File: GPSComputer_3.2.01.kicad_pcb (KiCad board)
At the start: 4 copper layers, 96 x 96 mm, 80 parts, among them J1 GPS_ANT_0, J2 GPS_ANT_0, J3 GPS_ANT_0, J4 2125281600, J5 Conn_02x08_Odd_Even, J6 Conn_02x08_Odd_Even, J7 GPS_ANT_0, U1 MAX-M10S-00B, U2 MAX-M10S-00B, U3 MAX-M10S-00B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

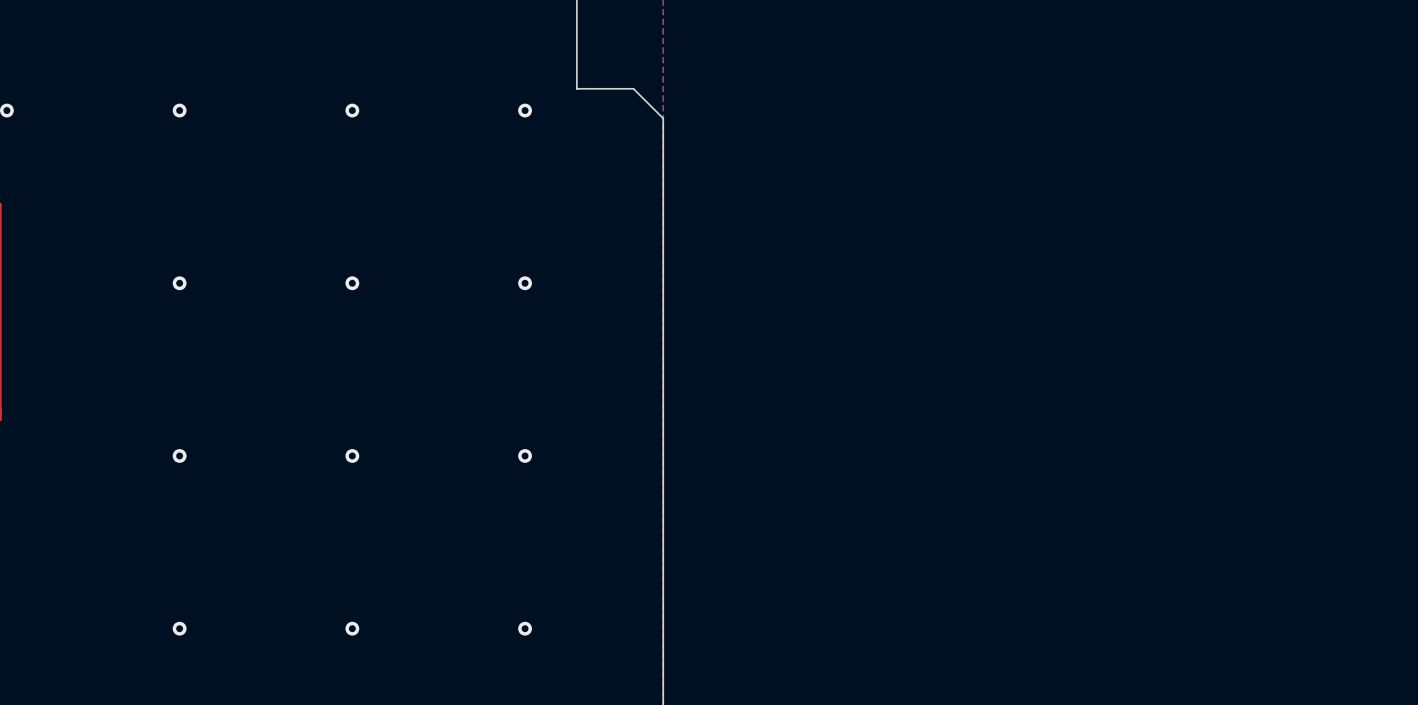
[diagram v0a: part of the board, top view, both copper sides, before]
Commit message: Adding RF
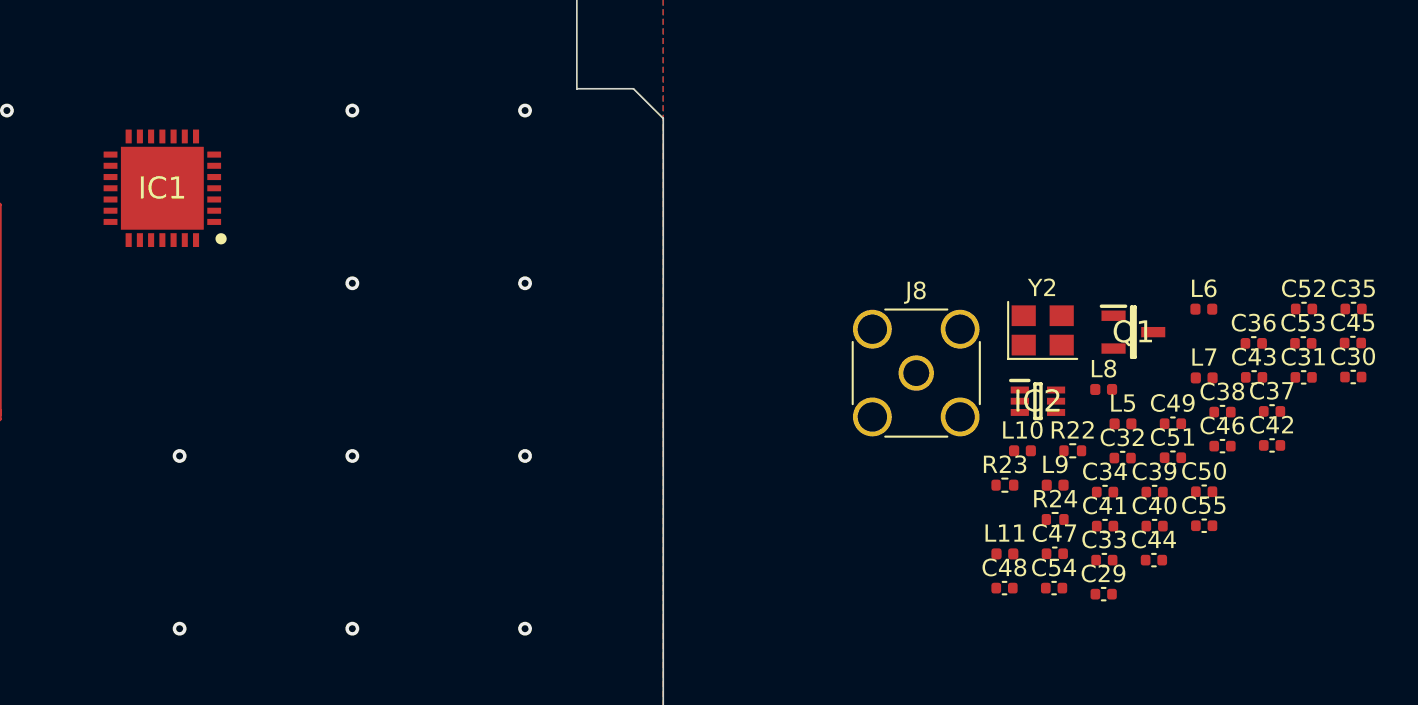
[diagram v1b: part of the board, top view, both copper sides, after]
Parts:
- added C29: 18pF, Capacitor_SMD:C_0402_1005Metric, F.Cu at (223.5, 128.0)
- added C30: 18pF, Capacitor_SMD:C_0402_1005Metric, F.Cu at (237.9, 115.4)
- added C31: 100nF, Capacitor_SMD:C_0402_1005Metric, F.Cu at (235.1, 115.5)
- added C32: 100nF, Capacitor_SMD:C_0402_1005Metric, F.Cu at (224.6, 120.1)
- added C33: 100nF, Capacitor_SMD:C_0402_1005Metric, F.Cu at (223.5, 126.0)
- added C34: 47pF, Capacitor_SMD:C_0402_1005Metric, F.Cu at (223.6, 122.1)
- added C35: 100nF, Capacitor_SMD:C_0402_1005Metric, F.Cu at (238.0, 111.5)
- added C36: 47pF, Capacitor_SMD:C_0402_1005Metric, F.Cu at (232.2, 113.5)
- added C37: 47pF, Capacitor_SMD:C_0402_1005Metric, F.Cu at (233.2, 117.4)
- added C38: 100nF, Capacitor_SMD:C_0402_1005Metric, F.Cu at (230.4, 117.5)
- added C39: NC, Capacitor_SMD:C_0402_1005Metric, F.Cu at (226.4, 122.1)
- added C40: 10nF, Capacitor_SMD:C_0402_1005Metric, F.Cu at (226.4, 124.1)
- added C41: 47pF, Capacitor_SMD:C_0402_1005Metric, F.Cu at (223.6, 124.1)
- added C42: 10pF, Capacitor_SMD:C_0402_1005Metric, F.Cu at (233.2, 119.4)
- added C43: 1.2pF, Capacitor_SMD:C_0402_1005Metric, F.Cu at (232.2, 115.5)
- added C44: 47pF, Capacitor_SMD:C_0402_1005Metric, F.Cu at (226.4, 126.0)
- added C45: 1.0nF, Capacitor_SMD:C_0402_1005Metric, F.Cu at (237.9, 113.5)
- added C46: 15pF, Capacitor_SMD:C_0402_1005Metric, F.Cu at (230.4, 119.4)
- added C47: 1.5pF, Capacitor_SMD:C_0402_1005Metric, F.Cu at (220.7, 125.7)
- added C48: 10pF, Capacitor_SMD:C_0402_1005Metric, F.Cu at (217.8, 127.7)
- added C49: 3.3pF, Capacitor_SMD:C_0402_1005Metric, F.Cu at (227.5, 118.1)
- added C50: 6.8pF, Capacitor_SMD:C_0402_1005Metric, F.Cu at (229.3, 122.1)
- added C51: 100pF, Capacitor_SMD:C_0402_1005Metric, F.Cu at (227.5, 120.1)
- added C52: 100pF, Capacitor_SMD:C_0402_1005Metric, F.Cu at (235.1, 111.5)
- added C53: 47pF, Capacitor_SMD:C_0402_1005Metric, F.Cu at (235.1, 113.5)
- added C54: NC, Capacitor_SMD:C_0402_1005Metric, F.Cu at (220.6, 127.7)
- added C55: NC, Capacitor_SMD:C_0402_1005Metric, F.Cu at (229.3, 124.0)
- added IC1: SX1278IMLTRT, SX1278_IC:QFN65P600X600X100-29N-D, F.Cu at (169.0, 104.5)
- added IC2: PE4259, PE4259:SOT65P210X110-6N, F.Cu at (219.7, 116.8)
- added J8: Antena_Coaxial, Connector_Coaxial:SMA_Amphenol_132134-16_Vertical, F.Cu at (212.7, 115.2)
- added L10: 10nH, Inductor_SMD:L_0402_1005Metric, F.Cu at (218.8, 119.7)
- added L11: 0R, Inductor_SMD:L_0402_1005Metric, F.Cu at (217.8, 125.7)
- added L5: 18nH, Inductor_SMD:L_0402_1005Metric, F.Cu at (224.6, 118.1)
- added L6: 4.3nH, Inductor_SMD:L_0402_1005Metric, F.Cu at (229.3, 111.5)
- added L7: 18nH, Inductor_SMD:L_0402_1005Metric, F.Cu at (229.3, 115.5)
- added L8: 47nH, Inductor_SMD:L_0402_1005Metric, F.Cu at (223.5, 116.2)
- added L9: 12nH, Inductor_SMD:L_0402_1005Metric, F.Cu at (220.7, 121.7)
- added Q1: 2SC3356-T1B-A_AS, 2SC3356:SOT95P280X140-3N, F.Cu at (225.2, 112.8)
- added R22: 10K, Resistor_SMD:R_0402_1005Metric, F.Cu at (221.7, 119.7)
- added R23: 1K, Resistor_SMD:R_0402_1005Metric, F.Cu at (217.8, 121.7)
- added R24: 1M, Resistor_SMD:R_0402_1005Metric, F.Cu at (220.7, 123.7)
- added Y2: 32MHz, Crystal:Crystal_SMD_3225-4Pin_3.2x2.5mm, F.Cu at (220.0, 112.7)
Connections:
- U7 pad 24: unconnected-(U7-Pad24) -> GPS_SX_TX_DIO0
- U7 pad 25: unconnected-(U7-Pad25) -> GPS_SX_TX_DIO1
- U7 pad 26: unconnected-(U7-Pad26) -> GPS_SX_TX_DIO2
- U7 pad 27: unconnected-(U7-Pad27) -> GPS_SX_TX_RESET
- U7 pad 33: unconnected-(U7-Pad33) -> GPS_SX_TX_SPI2_CS
- U7 pad 34: GPS2_RESET -> GPS_SX_TX_SPI2_SCK
- U7 pad 35: unconnected-(U7-Pad35) -> GPS_SX_TX_SPI2_MISO
- U7 pad 36: unconnected-(U7-Pad36) -> GPS_SX_TX_SPI2_MOSI
- U7 pad 39: unconnected-(U7-Pad39) -> GPS2_RESET
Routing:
- net GPS_SX_TX_SPI2_SCK: track 0.00 -> 32.0 mm
- net GPS2_RESET: track 32.0 -> 0.00 mm
- net GND: vias 501 -> 499
